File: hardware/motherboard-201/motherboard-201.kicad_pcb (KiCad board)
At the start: 2 copper layers, 216 x 150 mm, 108 parts, among them J1 PWR_conn, J2 DB25M, J3 MSX_Slot, J4 MSX_Slot, J5 GFX_Connector_Output, J6 CONN_JOY, J7 CONN_JOY, J8 DIN8, K1 Relay, Q2 2N2907, U1 AS6C1008, U10 74HC04, U11 74HC32, U12 74HC32, U13 74HC32, U14 74HC08, U15 74HC139, U16 74LS07, U17 74HC74, U19 LM311, U2 TL7705, U20 SST39SF0, U21 74HC138, U22 74HC138, U23 74HC157, U24 AY-3-8910, U25 74HC157, U26 74HC138, U27 74HC153, U28 82C55A, U6 Z84C00, U7 74HC74, U8 74HCT245

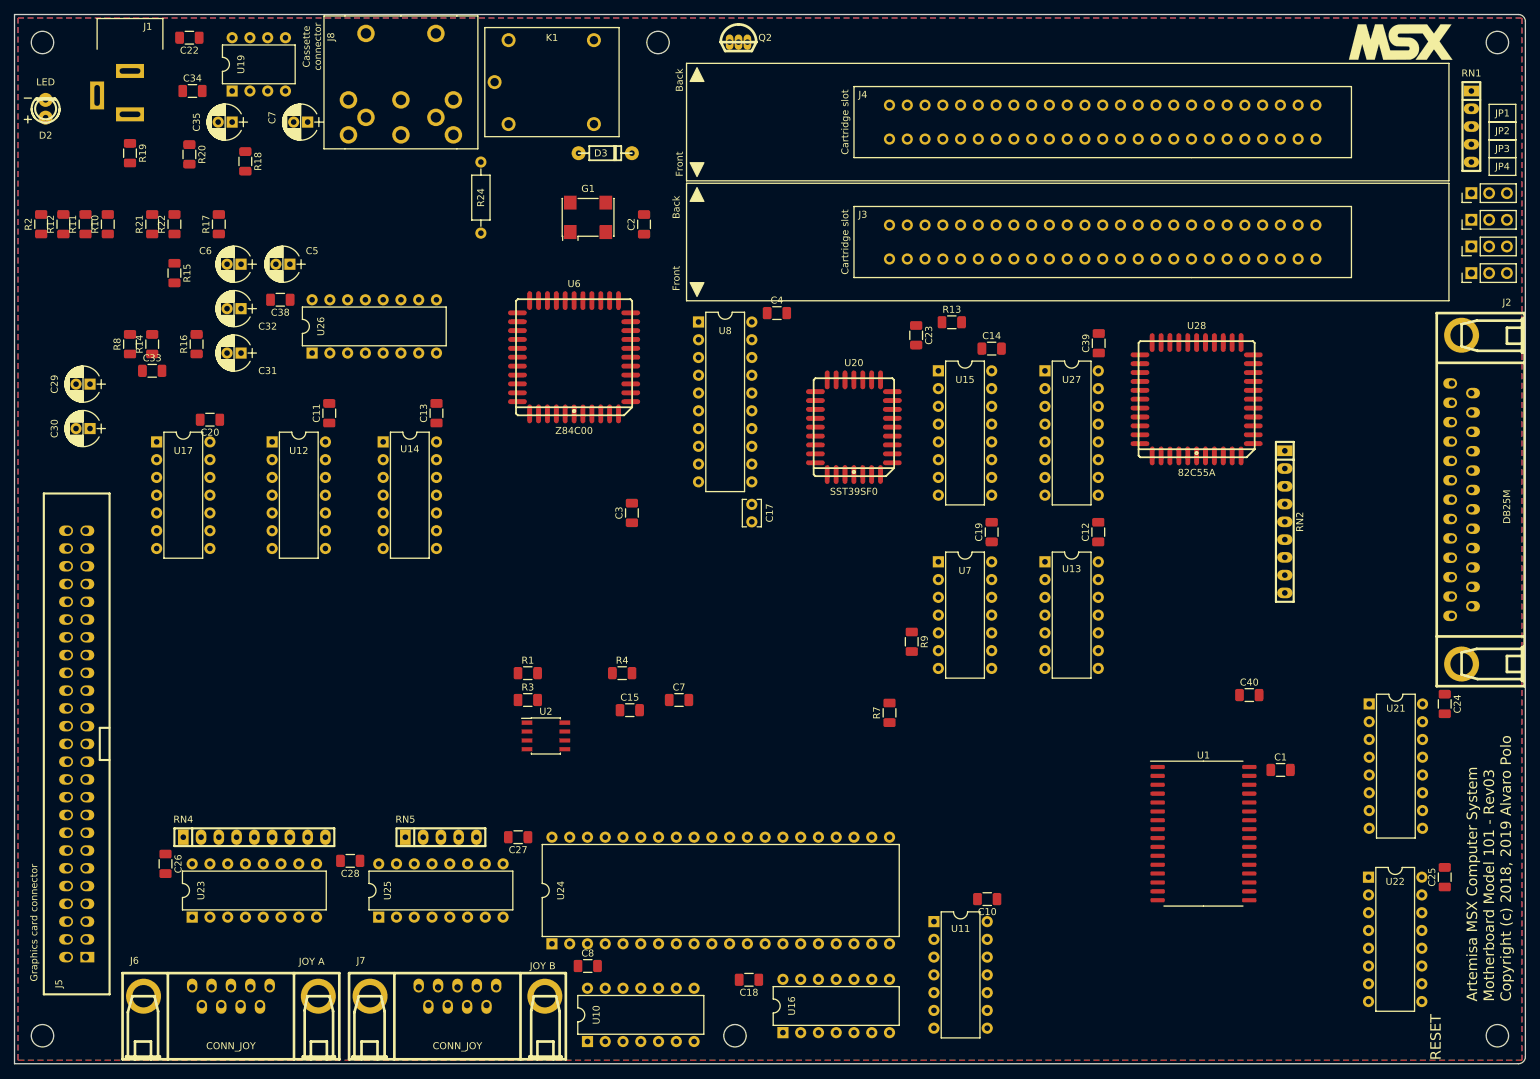
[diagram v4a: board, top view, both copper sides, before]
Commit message: Replace logic gates by a GAL in decoding logic
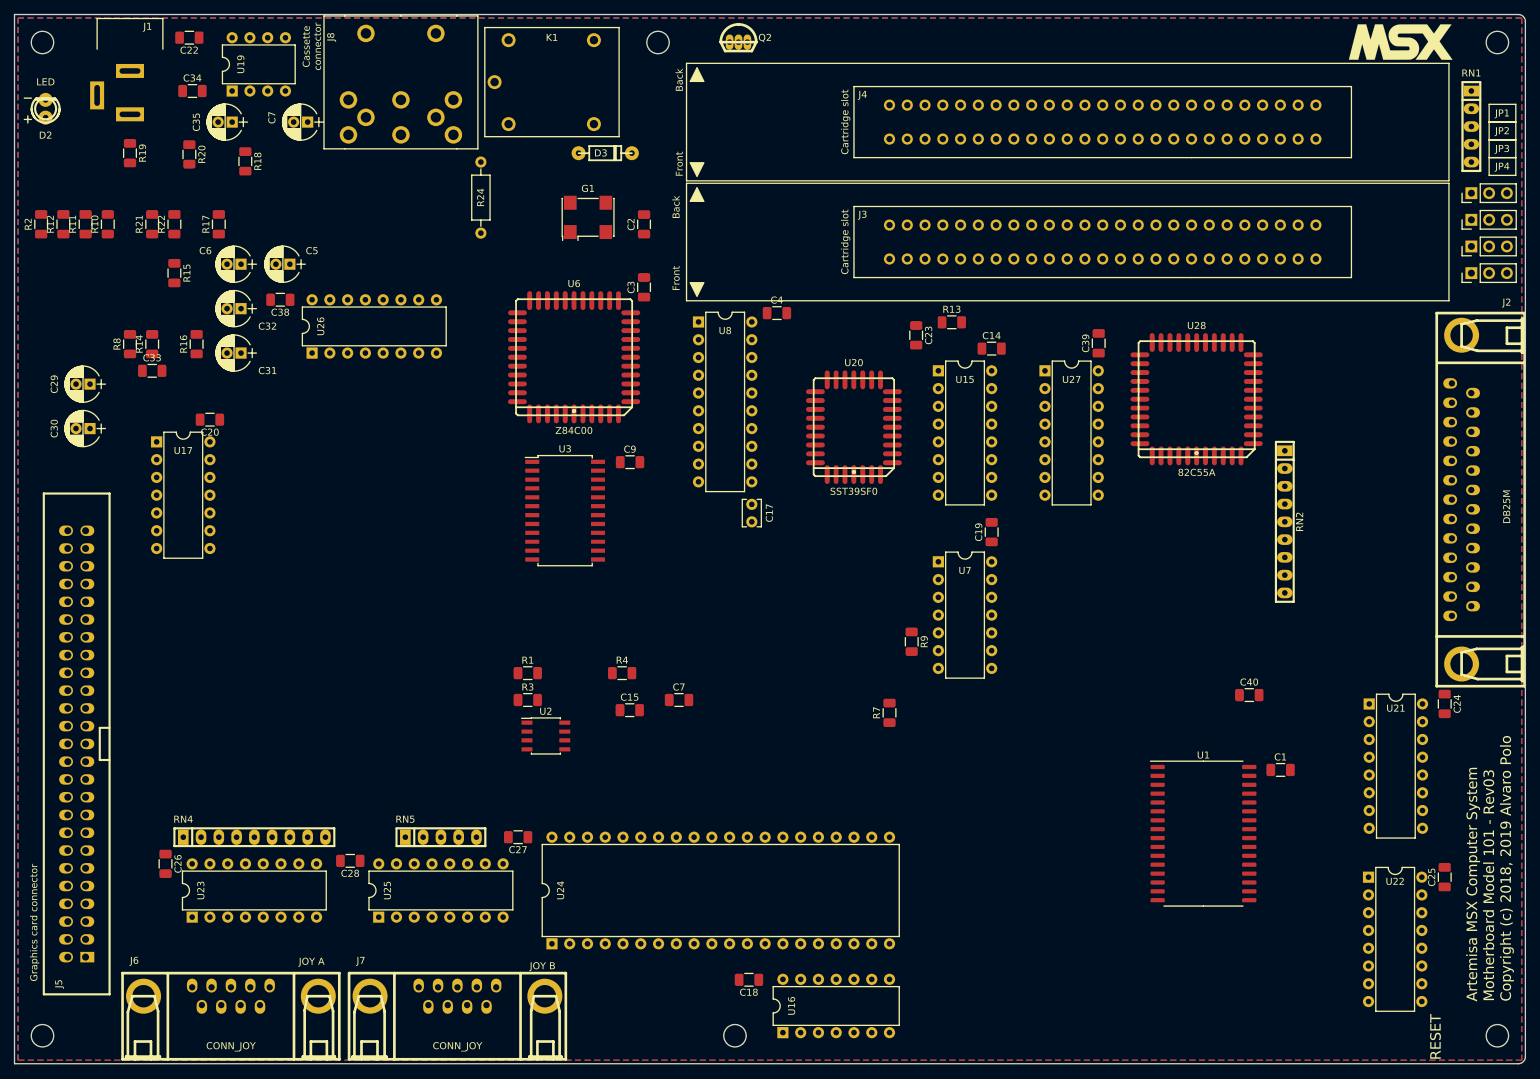
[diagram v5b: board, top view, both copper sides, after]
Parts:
- removed C10, C11, C12, C13, C8: 100nF, artemisa:C_1206
- removed U10: 74HC04, artemisa:DIP-14_300
- removed U11, U12, U13: 74HC32, artemisa:DIP-14_300
- removed U14: 74HC08, artemisa:DIP-14_300
- added C9: 100nF, artemisa:C_1206, F.Cu at (144.9, 142.6)
- added U3: GAL_declogic-201, artemisa:SOIC-24, F.Cu at (135.6, 149.5)
- moved C3 32.3 mm to (146.9, 117.6)
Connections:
- U15 pad 10: /~CS2 -> (no net)
- U15 pad 11: /~CS1 -> (no net)
- U15 pad 12: Net-(U15-Pad12) -> (no net)
- U15 pad 13: /ADDR15 -> (no net)
- U15 pad 14: /ADDR14 -> (no net)
- U15 pad 15: /~RD -> (no net)
- U15 pad 9: Net-(U15-Pad9) -> (no net)
- U26 pad 4: Net-(U13-Pad3) -> /DECODING/~IOSL
- U26 pad 5: /~IORQ -> /CPU/ADDR6
- U26 pad 6: /~M1 -> /CPU/ADDR7

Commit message: Use SOIC packages for remaining logic ICs that used DIP
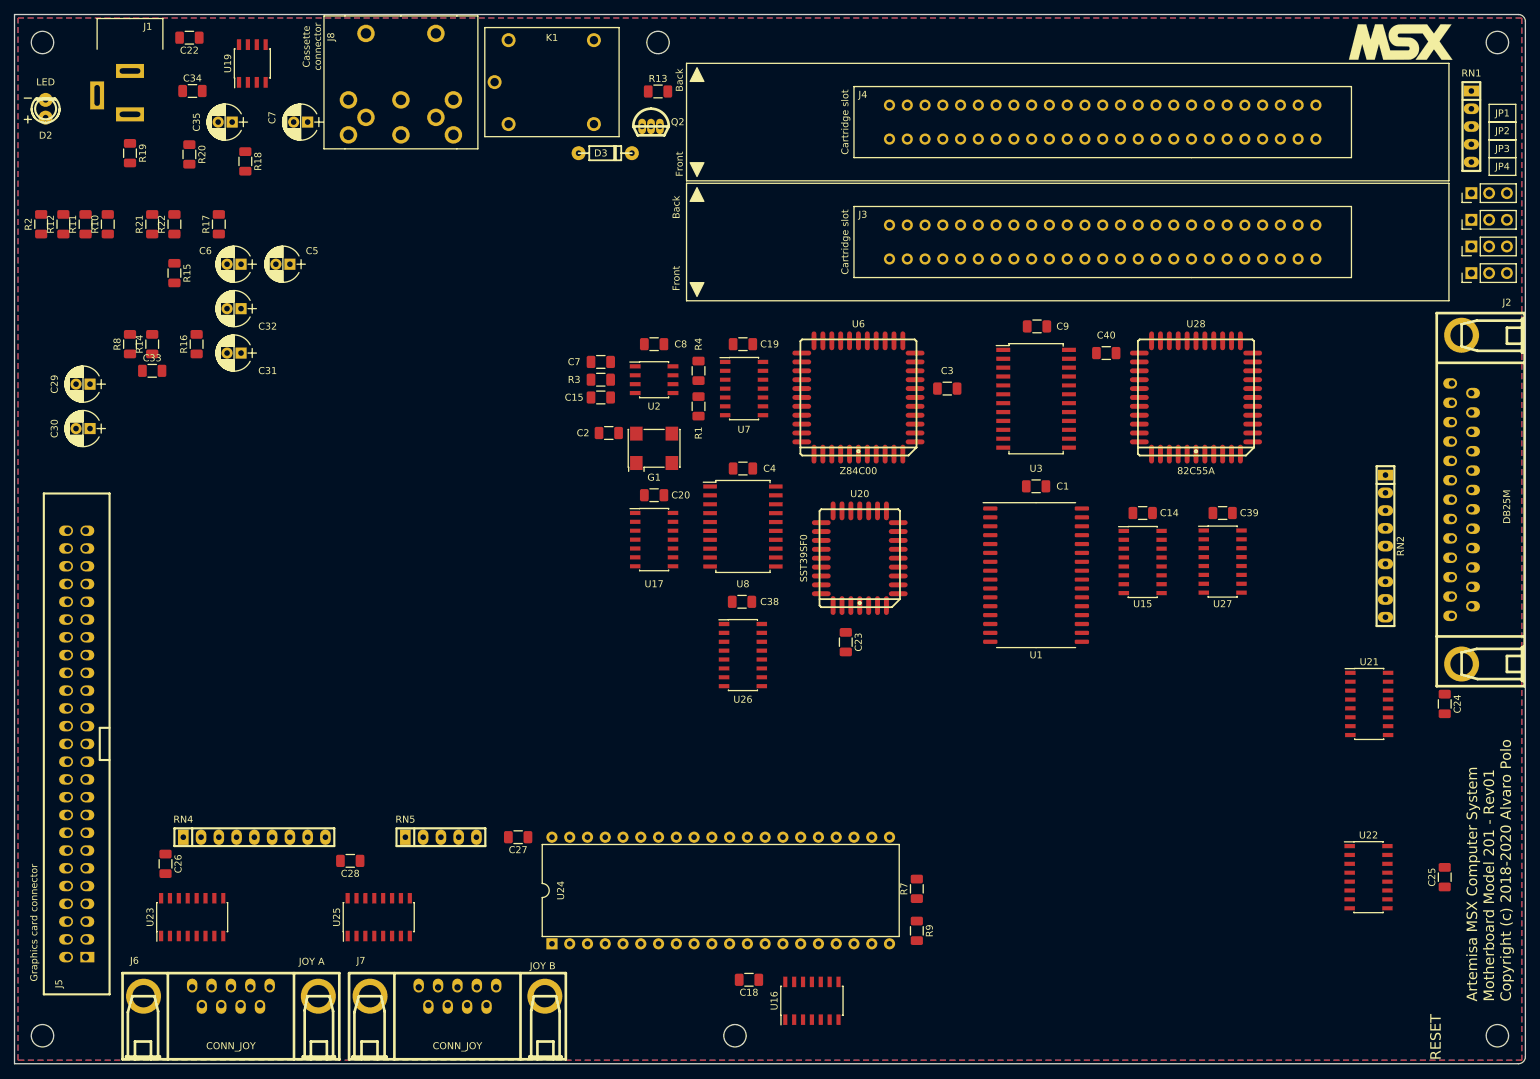
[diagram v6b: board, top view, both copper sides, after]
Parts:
- removed C17: 100nF, artemisa:Disc_capacitor
- removed R24: 1K, artemisa:Axial_resistor
- added C8: 100nF, artemisa:C_1206, F.Cu at (148.3, 125.7)
- U15, U21, U22, U23, U25, U26, U27: footprint artemisa:DIP-16_300 -> artemisa:SOIC-16
- U16, U17, U7: footprint artemisa:DIP-14_300 -> artemisa:SOIC-14
- U19: footprint artemisa:DIP-8_300 -> artemisa:SOIC-8_150
- U8: footprint artemisa:DIP-20_300 -> artemisa:SOIC-20
- moved C38 78.9 mm to (160.9, 162.6)
- moved U26 75.2 mm to (161.0, 170.2), turned to 0 degrees
- moved U17 72.5 mm to (148.3, 153.7)
- moved U3 69.2 mm to (202.9, 133.5)
- moved C20 64.4 mm to (148.3, 147.3)
- moved C9 61.3 mm to (203.1, 123.2), turned to 180 degrees
- moved C1 53.5 mm to (202.9, 146.1), turned to 180 degrees
- moved R13 53.4 mm to (148.9, 89.6)
- moved U2 53.2 mm to (148.3, 130.8)
- moved C40 53.0 mm to (213.0, 127.0), turned to 180 degrees
- moved C7 49.6 mm to (140.7, 128.3), turned to 180 degrees
- moved R3 47.0 mm to (140.7, 130.8)
- moved C3 45.7 mm to (190.2, 132.1), turned to 0 degrees
- moved R1 45.3 mm to (154.7, 134.6), turned to 90 degrees
- moved C23 45.0 mm to (175.7, 168.3)
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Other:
- board text added: "Artemisa MSX Computer System Motherboard Model 201 - Rev01 Copyright (c) 2018-2020 Alvaro Polo"
- board text removed: "Artemisa MSX Computer System Motherboard Model 101 - Rev03 Copyright (c) 2018, 2019 Alvaro Polo"

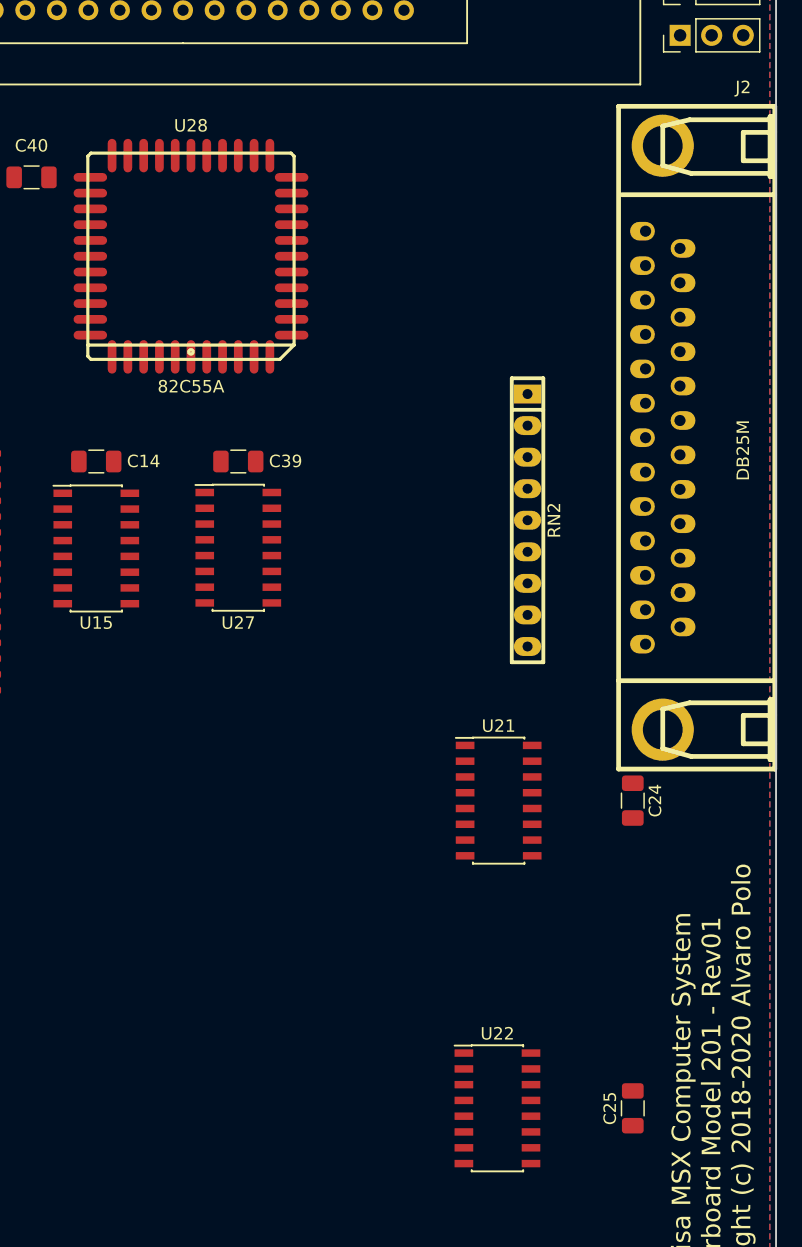
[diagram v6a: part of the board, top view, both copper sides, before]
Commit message: [mb201] Add a new circuit for PS2 keyboard
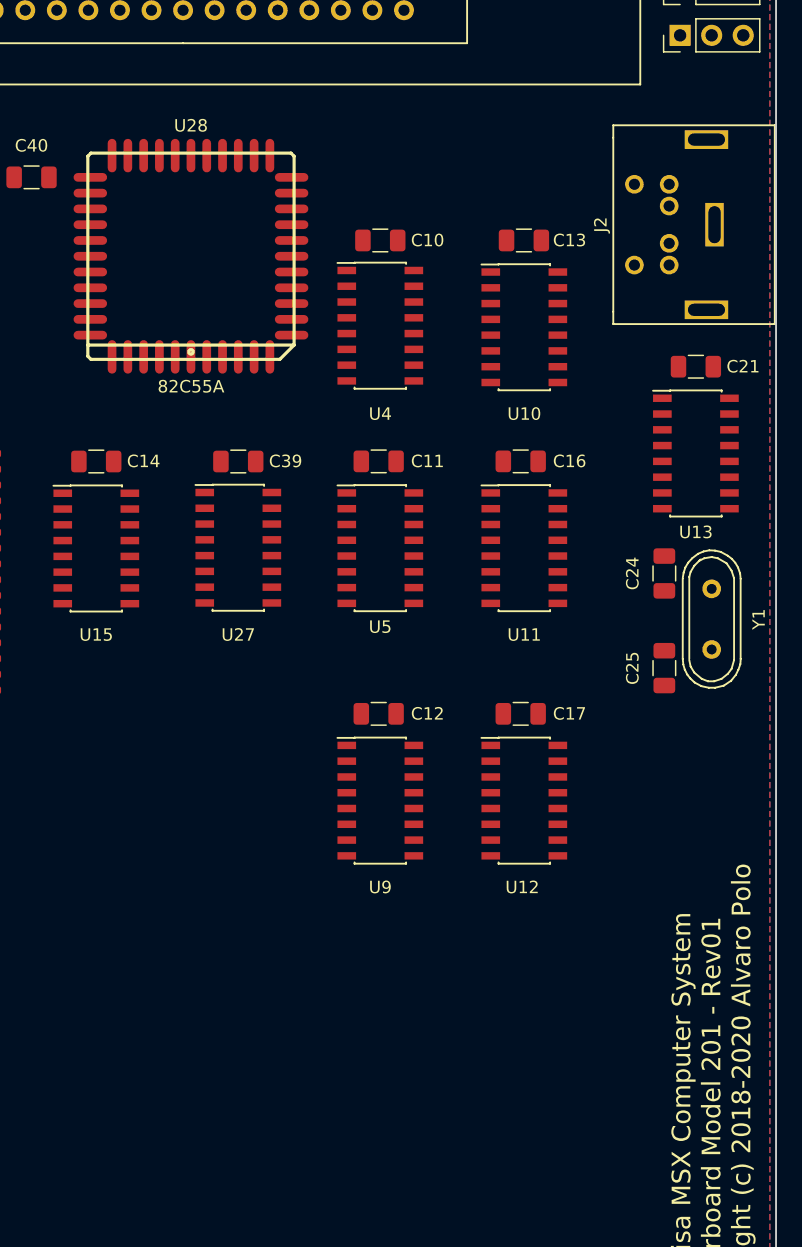
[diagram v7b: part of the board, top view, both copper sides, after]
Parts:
- removed RN2: 10K, artemisa:RN8
- removed U21, U22: 74HC138, artemisa:SOIC-16
- added C10: 0.1uF, artemisa:C_1206, F.Cu at (241.0, 132.1)
- added C11: 0.1uF, artemisa:C_1206, F.Cu at (240.9, 149.9)
- added C12: 0.1uF, artemisa:C_1206, F.Cu at (240.9, 170.2)
- added C13: 0.1uF, artemisa:C_1206, F.Cu at (252.6, 132.1)
- added C16: 0.1uF, artemisa:C_1206, F.Cu at (252.3, 149.9)
- added C17: 0.1uF, artemisa:C_1206, F.Cu at (252.3, 170.2)
- added C21: 0.1uF, artemisa:C_1206, F.Cu at (266.4, 142.2)
- added U10: 74HC670, artemisa:SOIC-16, F.Cu at (252.6, 139.1)
- added U11: 74HC670, artemisa:SOIC-16, F.Cu at (252.6, 156.8)
- added U12: 74HC670, artemisa:SOIC-16, F.Cu at (252.6, 177.2)
- added U13: ATMEGA328P, artemisa:SOIC-16, F.Cu at (266.4, 149.2)
- added U4: 74HC670, artemisa:SOIC-16, F.Cu at (241.0, 138.9)
- added U5: 74HC670, artemisa:SOIC-16, F.Cu at (241.0, 156.8)
- added U9: 74HC670, artemisa:SOIC-16, F.Cu at (241.0, 177.2)
- added Y1: 16Mhz, artemisa:Crystal, F.Cu at (267.7, 162.6)
- C24, C25: value 100nF -> 33pF
- J2: value DB25M -> PS2_CONN; footprint artemisa:DB25M -> artemisa:PS2_conn
- moved C25 35.5 mm to (263.9, 166.5)
- moved C24 18.5 mm to (263.9, 158.9)
- moved J2 17.3 mm to (272.8, 130.8)
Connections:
- C24 pad 1: ~ -> GND
- C24 pad 2: GND -> Net-(C24-Pad2)
- C25 pad 1: ~ -> GND
- C25 pad 2: GND -> Net-(C25-Pad2)
- J2 pad 1: /KBD/KBCOL0 -> Net-(J2-Pad1)
- J2 pad 2: /KBD/KBCOL1 -> Net-(J2-Pad2)
- J2 pad 3: /KBD/KBCOL2 -> GND
- J2 pad 4: /KBD/KBCOL3 -> ~
- J2 pad 5: /KBD/KBCOL4 -> Net-(J2-Pad5)
- J2 pad 6: /KBD/KBCOL5 -> Net-(J2-Pad6)
- U15 pad 10: (no net) -> /KBD/~RSL2
- U15 pad 11: (no net) -> /KBD/~RSL1
- U15 pad 12: (no net) -> /KBD/~RSL0
- U15 pad 13: (no net) -> /KBD/KBROW3
- U15 pad 14: (no net) -> /KBD/KBROW2
- U15 pad 15: (no net) -> GND
- U15 pad 9: (no net) -> Net-(U15-Pad9)
- U16 pad 10: /KBD/~CAPSL -> (no net)
- U16 pad 11: /~CAPSLOCK -> (no net)
- U16 pad 12: /KBD/~KANAL -> (no net)
- U16 pad 13: /~KANALOCK -> (no net)

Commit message: Remove jumper selectors for ROM image
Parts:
- removed JP1, JP2, JP3, JP4: Jumper, artemisa:Jumper
- removed RN1: 10K, artemisa:RN4
